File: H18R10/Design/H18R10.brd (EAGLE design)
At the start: 60 x 34.6 mm, 35 parts, among them P2 HEXABIT_X2_P1_P5, U1 STM32G0B1CEU6NUFQFPN48_STM32_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, U2 L298P, U3 MC7805CD2TR4G, X1 XTALL_CSTCE8M00G52

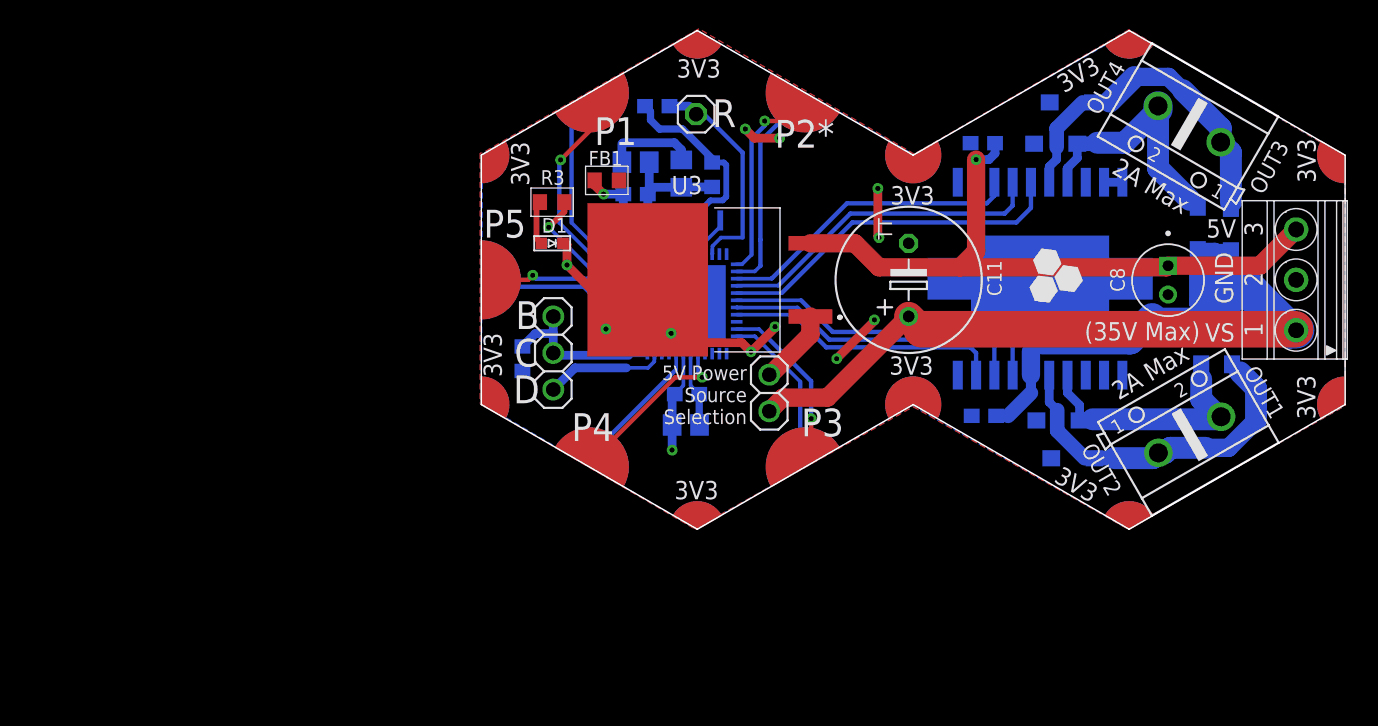
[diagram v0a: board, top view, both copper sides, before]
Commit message: -Adding a heatsink - replace the MC7805 with LM2775 IC
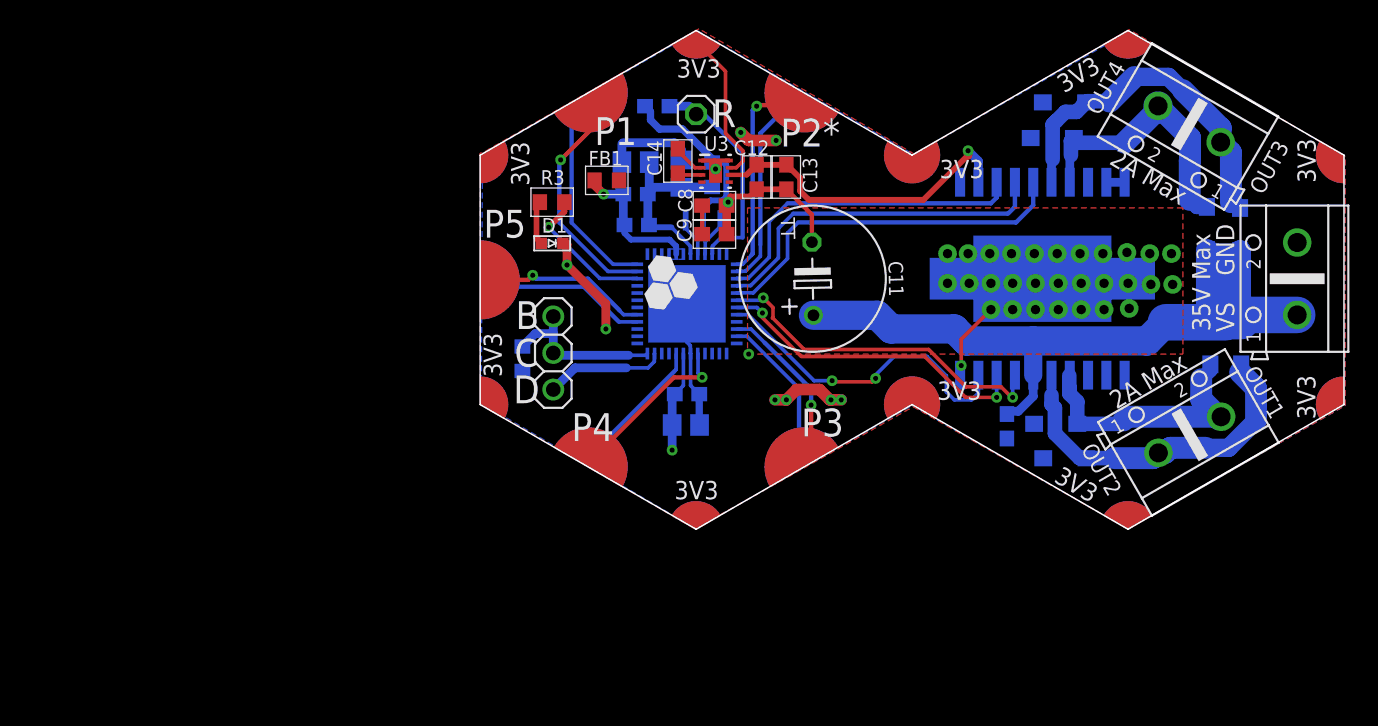
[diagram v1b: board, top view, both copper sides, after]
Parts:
- removed JP3: (no value), pinhead:1X02
- removed PWR: 1751251, HEXABITZ_CONNECTION_PARTS:1751251
- added C12: 100nF, HEXABITZ_RCLS:C-0603
- added C13: 10uF, HEXABITZ_RCLS:C-0603
- added C14: 1uF, HEXABITZ_RCLS:C-0603
- added POWER: (no value), HEXABITZ_CONNECTION_PARTS:AK500/2
- C8: value 100uF/10V -> 100nF; device HEXABITZ_RCLS:CAPPRD200W50D500H1100 -> HEXABITZ_RCLS:C-0603
- C9: value 100nF -> 10uF
- U3: value MC7805CD2TR4G -> LM2775-Q1; device HEXABITZ_ICs:MC7805CD2TR4G -> HEXABITZ_ICs:DSG0008A
- moved C8 31.9 mm to (16.1, 25.5), turned to 0 degrees
- moved C9 19.7 mm to (16.1, 23.5), flipped to the top
- moved U3 10.0 mm to (16.2, 27.9), turned to 0 degrees
- moved C11 6.67 mm to (22.9, 20.4), turned to 91.2 degrees
- moved C10 1.75 mm to (36.4, 10.2), turned to 270 degrees
- moved D3 0.64 mm to (50.3, 23.9)
- moved D2 0.63 mm to (52.6, 23.8)
- moved D4 0.63 mm to (52.7, 16.0)
- moved D5 0.63 mm to (50.6, 16.0)
- moved D9 0.56 mm to (40.5, 7.93)
- moved D7 0.48 mm to (40.4, 32.6)
- moved D6 0.46 mm to (39.6, 30.2)
- moved D8 0.29 mm to (39.8, 10.3)
- moved U2 0.16 mm to (38.9, 20.4)
- moved P2 0.08 mm to (30.1, 20.3)
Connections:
- removed net N$12: JP3.2, U3.1
- new net N$3: C14.2, U3.2
- new net N$4: C14.1, U3.3
- net +5V: now also C12.1, C13.1, U3.6; no longer C8.P, C9.1, PWR.3, U3.3
- net GND: now also C12.2, C13.2, C8.2, POWER.2, U1.24, U1.25, U3.1, U3.8, U3.9; no longer C8.N, PWR.2, U3.2
- net V+: now also POWER.1; no longer JP3.1, PWR.1
- net VDD: now also C8.1, C9.1, U3.4, U3.5, U3.7
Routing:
- net +5V: track 47.9 -> 22.5 mm
- net V+: track 84.5 -> 65.6 mm
- net VDD: track 7.18 -> 20.3 mm
- net N$12: track 5.28 -> 0.00 mm
- net IN2: track 19.3 -> 23.1 mm, vias 0 -> 2
- net N$3: track 0.00 -> 2.29 mm
- net GND: track 58.8 -> 56.9 mm, vias 11 -> 41
- net N$4: track 0.00 -> 1.72 mm
- net IN1: track 22.6 -> 24.3 mm, vias 0 -> 2
- net IN3: track 21.2 -> 22.9 mm
- net ENB: track 23.1 -> 24.5 mm
- net ENA: track 21.0 -> 22.4 mm, vias 0 -> 2
- net N$16: track 18.4 -> 19.6 mm
- net IN4: track 24.7 -> 25.8 mm
- net USART2_TX: track 14.1 -> 15.0 mm
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- added copper zone on layer 1, net GND
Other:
- board text removed: "(35V Max)"
- board text removed: "5V"
- board text removed: "5V Power Source Selection"

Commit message: -Improving the layout desin and adding TVSs at the MCU GPIOs that connected to the driver IC inputs, and across its supply pins all to increase the imunity against the high spikes.
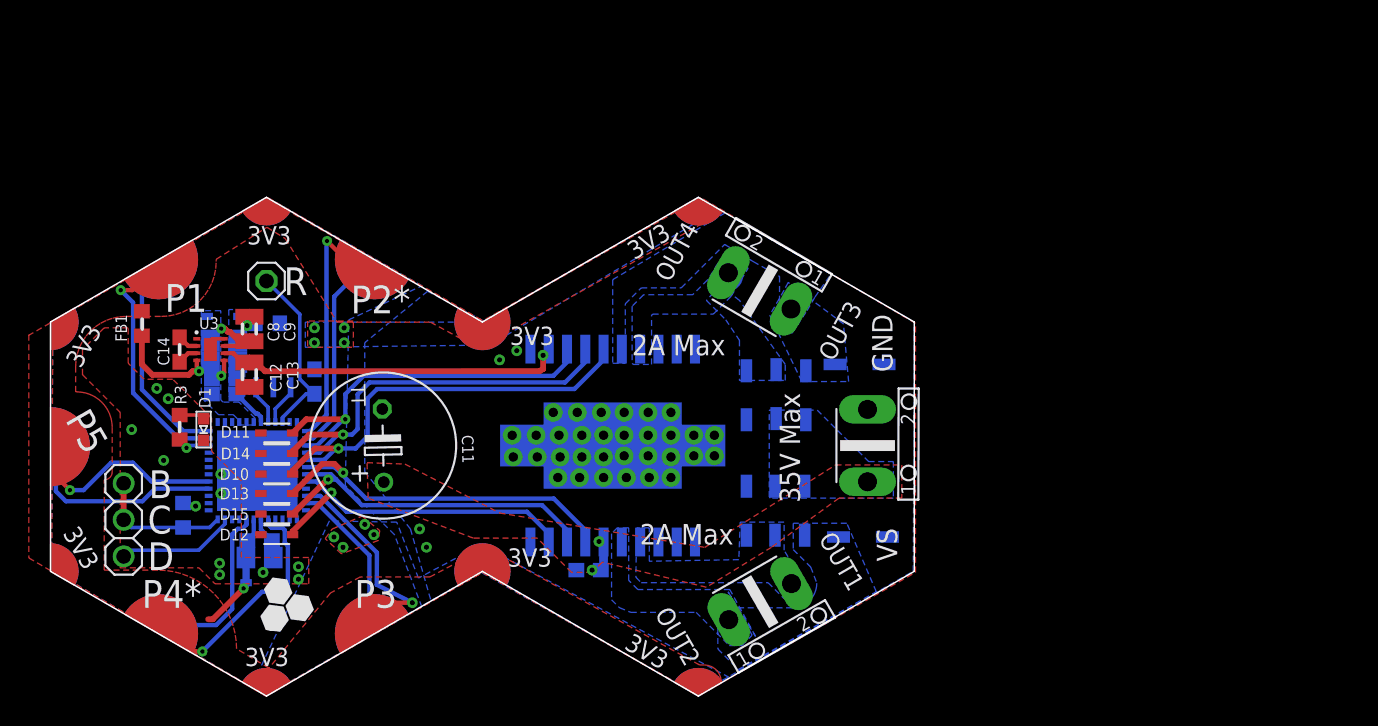
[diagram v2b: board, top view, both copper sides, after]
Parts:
- added D10, D11, D12, D13, D14, D15, D16, D17: BOURNS_CDSOD323-T03SCBOURNS_CDSOD323-T03SC_0_0, HEXABITZ_RCLS:BOURNS_CDSOD323-T03SC_0
- D1: value VLMS1300-GS08 -> RED
- D2, D3, D4, D5, D6, D7, D8, D9: value MBR120ESFT1G -> DIOD-SOD-123; device HEXABITZ_RCLS:SODFL3616X98N -> HEXABITZ_RCLS:SOD123
- P2: value HEXABIT_X2_P1_P5 -> HEXABIT_X2_P1_P5_EDIT_POWER_PADS; device hexabitz_connectors:HEXABIT_17.32_X2_P1_P5 -> hexabitz_connectors:HEXABIT_X2_P1_P5_EDIT_POWER_PADS
- U1: value STM32G0B1CEU6NUFQFPN48_STM32_STM -> STM32G0B1CEU6N; device HEXABITZ_ICs:UFQFPN48_STM32_STM -> HEXABITZ_ICs:HEXABITZ_ICS_QFN_B1CEU6_STM-L
- moved C13 39.3 mm to (-15.7, 13.7)
- moved C12 38.3 mm to (-16.7, 13.7)
- moved D2 37.7 mm to (20.3, 4.29)
- moved U3 37.2 mm to (-18.9, 15.5)
- moved C14 37.0 mm to (-21.0, 15.5)
- moved C2 34.3 mm to (-17.9, 14.6), turned to 180 degrees
- moved D3 34.1 mm to (22.4, 4.29)
- moved C8 33.9 mm to (-16.7, 16.9), turned to 90 degrees
- moved FB1 33.8 mm to (-23.7, 17.3), turned to 90 degrees
- moved D6 33.5 mm to (18.3, 4.29), turned to 270 degrees
- moved D7 33.3 mm to (26.4, 2.46)
- moved R2 32.6 mm to (-14.9, 17.3), turned to 180 degrees
- moved C9 32.5 mm to (-15.7, 16.9), turned to 90 degrees
- moved C11 32.0 mm to (-6.91, 8.81)
- moved JP1 32.0 mm to (-15.0, 20.2)
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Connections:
- removed net N$16: D3.2, D6.1, M2.2, U2.17
- new net N$7: D5.1, D9.2, M2.2, U2.17
- net ENA: now also D15.2
- net ENB: now also D14.2
- net GND: now also D17.1; no longer C10.2, C11.-, C12.2, C13.2, C8.2, C9.2, D6.2, D7.2, D8.2, D9.2, P2.PAD_PD15, P2.PAD_PD16, POWER.2, U1.1, U1.2, U1.24, U1.25, U1.37, U1.38, U2.1, U2.10, U2.11, U2.19, U2.2, U2.20, U2.21, U2.22, U2.23, U3.1, U3.8, U3.9
- net IN1: now also D13.2
- net IN2: now also D12.2
- net IN3: now also D11.2
- net IN4: now also D10.2
- net N$13: now also D3.1, D7.2; no longer D4.2, D9.1
- net N$14: now also D4.1, D8.2; no longer D2.2, D7.1
- net N$15: now also D2.1, D6.2; no longer D5.2, D8.1
- net V+: now also D2.2, D3.2, D4.2, D5.2; no longer D2.1, D3.1, D4.1, D5.1
- net VDD: now also D17.2; no longer C8.1, C9.1, P2.PAD_PU15, P2.PAD_PU16, U3.4, U3.5, U3.7
- net VDDA: now also C8.1, C9.1, D16.2, U3.4, U3.5, U3.7
- net VSSA: now also C10.2, C11.-, C12.2, C13.2, C8.2, C9.2, D10.1, D11.1, D12.1, D13.1, D14.1, D15.1, D16.1, D6.1, D7.1, D8.1, D9.1, POWER.2, U2.1, U2.10, U2.11, U2.19, U2.2, U2.20, U2.21, U2.22, U2.23, U3.1, U3.8, U3.9
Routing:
- net V+: track 65.6 -> 2.41 mm, vias 0 -> 2
- net GND: track 56.9 -> 6.49 mm, vias 41 -> 20
- net N$14: track 25.0 -> 0.00 mm
- net N$13: track 24.3 -> 0.00 mm
- net N$16: track 19.6 -> 0.00 mm
- net N$15: track 18.7 -> 0.25 mm
- net VDD: track 20.3 -> 8.58 mm
- net VSSA: track 12.9 -> 4.35 mm, vias 0 -> 37
- net N$2: track 9.82 -> 2.38 mm
- net USART1_TX: track 11.7 -> 16.9 mm
- net IN4: track 25.8 -> 29.9 mm, vias 0 -> 1
- net ENB: track 24.5 -> 28.6 mm, vias 0 -> 1
- net IN3: track 22.9 -> 26.6 mm, vias 0 -> 1
- net USART3_TX: track 12.0 -> 15.2 mm
- net USART5_RX: track 11.4 -> 14.5 mm
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- added copper zone on layer 16, net N$13
- added copper zone on layer 16, net N$14
- added copper zone on layer 16, net N$15
- added copper zone on layer 16, net N$7
- added copper zone on layer 1, net V+
- added copper zone on layer 16, net V+
- added copper zone on layer 1, net VSSA
- added copper zone on layer 16, net VSSA
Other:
- board text added: "P4*"
- board text removed: "*P2"
- board text removed: "P4"
